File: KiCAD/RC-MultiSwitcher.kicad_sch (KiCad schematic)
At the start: 28 parts, among them IC1 LM2940IMP-5.0_NOPB, J1 Pwr_Outputs, J3 Srv_INPUTS, J4 Srv_OUTPUTS, Q1 DMG9926USD-13, Q2 DMG9926USD-13, Q3 DMG9926USD-13, U1 Teensy3.1

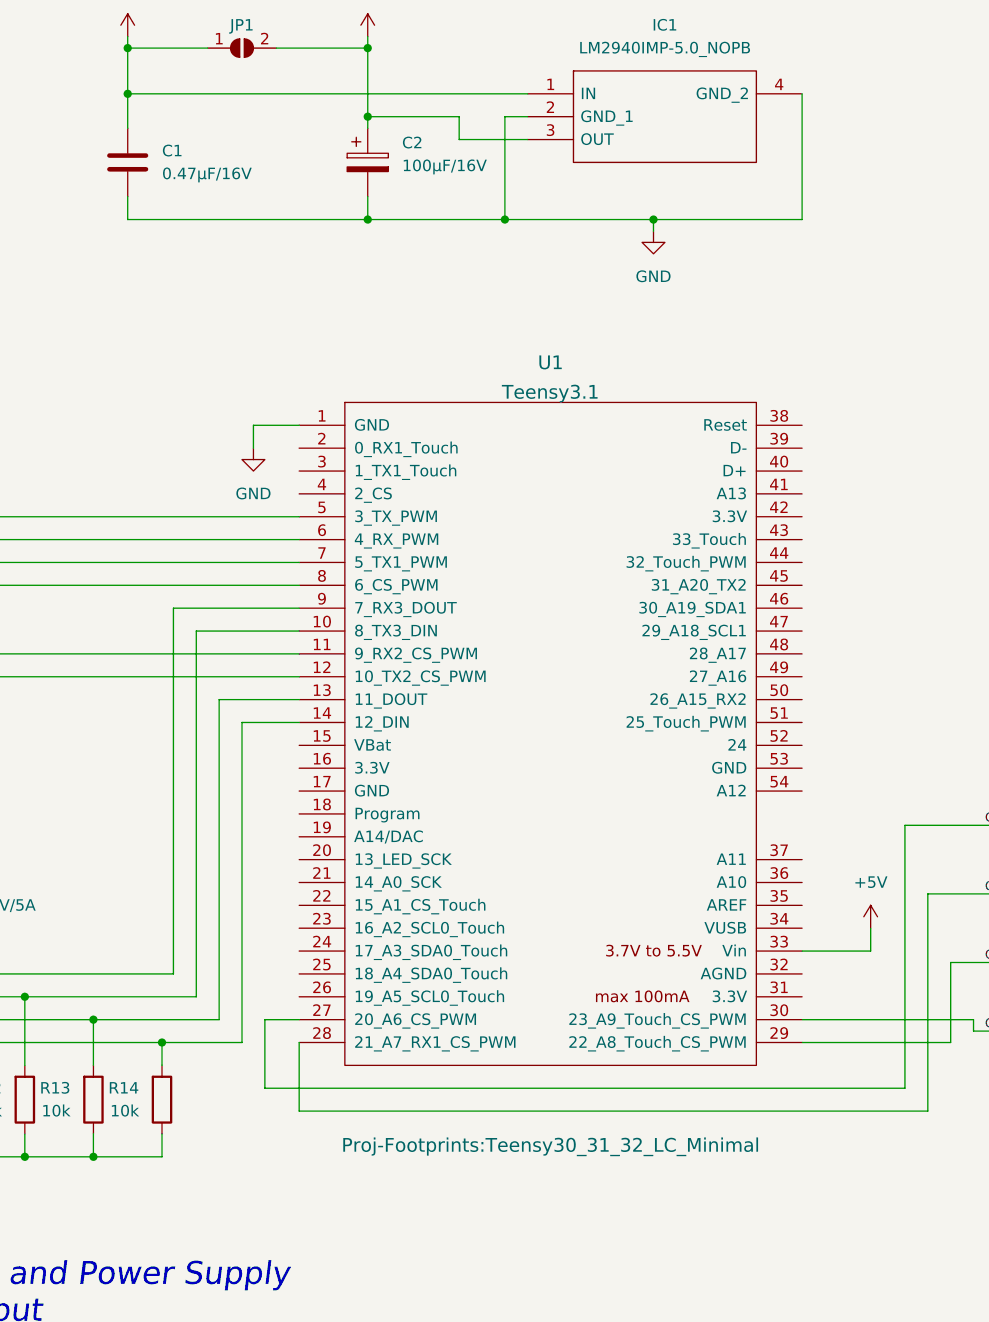
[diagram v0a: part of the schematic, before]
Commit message: minor layout improvements; added manufacturing data
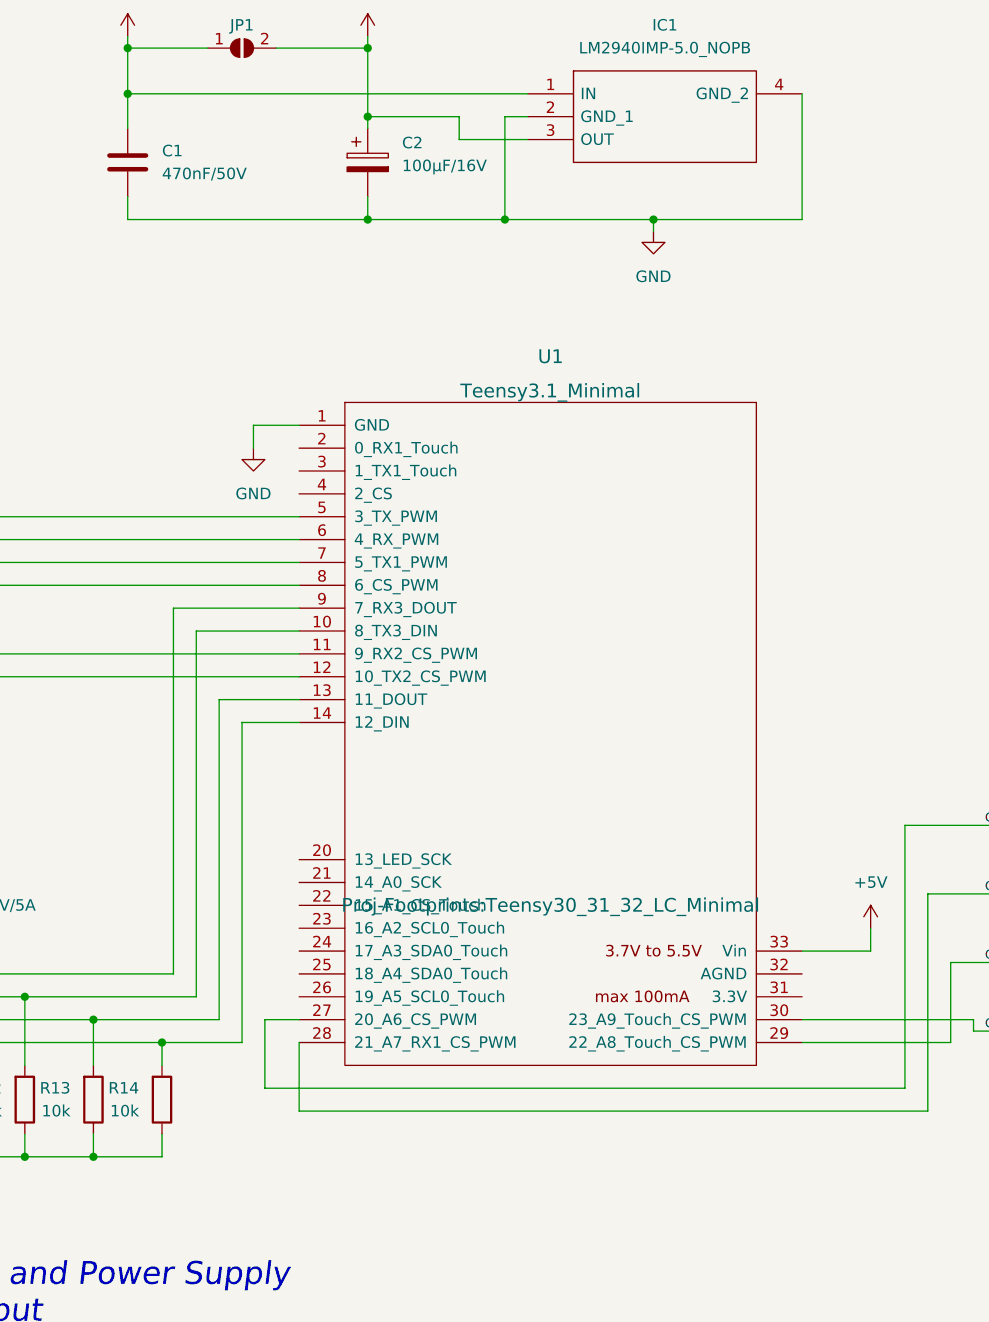
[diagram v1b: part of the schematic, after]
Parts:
- removed U1: Teensy3.1, Proj-Footprints:Teensy30_31_32_LC_Minimal, symbol Teensy3:Teensy3.1
- added U1: Teensy3.1_Minimal, Proj-Footprints:Teensy30_31_32_LC_Minimal, symbol Teensy3:Teensy3.1_Minimal
- C1: value 0.47µF/16V -> 470nF/50V; LCSC C106851 -> C77572
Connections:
- net +5V: now also U1.33 (Vin)
- net GND: now also U1.1 (GND)
- net I-SRV0: now also U1.9 (7_RX3_DOUT)
- net I-SRV1: now also U1.10 (8_TX3_DIN)
- net I-SRV2: now also U1.13 (11_DOUT)
- net I-SRV3: now also U1.14 (12_DIN)
- net O-SRV0: now also U1.27 (20_A6_CS_PWM)
- net O-SRV1: now also U1.28 (21_A7_RX1_CS_PWM)
- net O-SRV2: now also U1.29 (22_A8_Touch_CS_PWM)
- net O-SRV3: now also U1.30 (23_A9_Touch_CS_PWM)
- net at Q2.2 (G1), R3.2: now also U1.7 (5_TX1_PWM)
- net at Q3.4 (G2), R10.2: now also U1.12 (10_TX2_CS_PWM)
- net at Q3.2 (G1), R9.2: now also U1.11 (9_RX2_CS_PWM)
- net at Q1.2 (G1), R1.2: now also U1.5 (3_TX_PWM)
- net at Q1.4 (G2), R2.2: now also U1.6 (4_RX_PWM)
- net at Q2.4 (G2), R4.2: now also U1.8 (6_CS_PWM)

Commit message: minor update to PCB
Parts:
- added J2: Alt_Pwr, Connector_JST:JST_XH_B2B-XH-A_1x02_P2.50mm_Vertical, symbol Connector:Conn_01x02_Male
- added JP2: (no value), Jumper:SolderJumper-2_P1.3mm_Open_Pad1.0x1.5mm, symbol Jumper:SolderJumper_2_Open
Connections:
- net +6V: now also JP2.2 (B)
- net GND: now also J2.1 (Pin_1)
- net PWR-IN: now also J2.2 (Pin_2), JP2.1 (A)
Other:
- moved on the sheet: F1
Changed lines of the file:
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@@
   (junction (at 34.29 142.24) (diameter 0) (color 0 0 0 0)
   )
+  (junction (at 116.84 111.76) (diameter 0) (color 0 0 0 0)
+  )
   (junction (at 49.53 137.16) (diameter 0) (color 0 0 0 0)
   )
@@
   (junction (at 34.29 109.22) (diameter 0) (color 0 0 0 0)
   )
+  (junction (at 124.46 123.19) (diameter 0) (color 0 0 0 0)
+  )
   (junction (at 87.63 101.6) (diameter 0) (color 0 0 0 0)
   )
@@
   (junction (at 246.38 120.65) (diameter 0) (color 0 0 0 0)
   )
+  (junction (at 129.54 123.19) (diameter 0) (color 0 0 0 0)
+  )
   (junction (at 87.63 175.26) (diameter 0) (color 0 0 0 0)
   )
@@
   (junction (at 49.53 132.08) (diameter 0) (color 0 0 0 0)
   )
+  (wire (pts (xy 124.46 123.19) (xy 124.46 132.08))
+    (stroke (width 0) (type default) (color 0 0 0 0))
+  )
   (wire (pts (xy 248.92 106.68) (xy 248.92 115.57))
     (stroke (width 0) (type default) (color 0 0 0 0))
@@
     (stroke (width 0) (type default) (color 0 0 0 0))
   )
+  (wire (pts (xy 139.7 123.19) (xy 139.7 119.38))
+    (stroke (width 0) (type default) (color 0 0 0 0))
+  )
   (wire (pts (xy 87.63 83.82) (xy 162.56 83.82))
     (stroke (width 0) (type default) (color 0 0 0 0))
@@
     (stroke (width 0) (type default) (color 0 0 0 0))
   )
+  (wire (pts (xy 129.54 123.19) (xy 129.54 120.65))
+    (stroke (width 0) (type default) (color 0 0 0 0))
+  )
   (wire (pts (xy 52.07 170.18) (xy 49.53 170.18))
     (stroke (width 0) (type default) (color 0 0 0 0))
@@
     (stroke (width 0) (type default) (color 0 0 0 0))
   )
+  (wire (pts (xy 116.84 111.76) (xy 116.84 113.03))
+    (stroke (width 0) (type default) (color 0 0 0 0))
+  )
   (wire (pts (xy 251.46 118.11) (xy 229.87 118.11))
     (stroke (width 0) (type default) (color 0 0 0 0))
@@
     (stroke (width 0) (type default) (color 0 0 0 0))
   )
+  (wire (pts (xy 129.54 123.19) (xy 139.7 123.19))
+    (stroke (width 0) (type default) (color 0 0 0 0))
+  )
   (wire (pts (xy 80.01 106.68) (xy 77.47 106.68))
     (stroke (width 0) (type default) (color 0 0 0 0))
@@
     (stroke (width 0) (type default) (color 0 0 0 0))
   )
+  (wire (pts (xy 116.84 123.19) (xy 124.46 123.19))
+    (stroke (width 0) (type default) (color 0 0 0 0))
+  )
   (wire (pts (xy 78.74 170.18) (xy 77.47 170.18))
     (stroke (width 0) (type default) (color 0 0 0 0))
   )
+  (wire (pts (xy 129.54 111.76) (xy 116.84 111.76))
+    (stroke (width 0) (type default) (color 0 0 0 0))
+  )
   (wire (pts (xy 229.87 147.32) (xy 158.75 147.32))
     (stroke (width 0) (type default) (color 0 0 0 0))
@@
     (stroke (width 0) (type default) (color 0 0 0 0))
   )
+  (wire (pts (xy 142.24 119.38) (xy 142.24 127))
+    (stroke (width 0) (type default) (color 0 0 0 0))
+  )
   (wire (pts (xy 234.95 142.24) (xy 218.44 142.24))
     (stroke (width 0) (type default) (color 0 0 0 0))
@@
     (stroke (width 0) (type default) (color 0 0 0 0))
   )
-  (wire (pts (xy 124.46 132.08) (xy 124.46 129.54))
+  (wire (pts (xy 116.84 123.19) (xy 116.84 120.65))
     (stroke (width 0) (type default) (color 0 0 0 0))
   )
@@
     (stroke (width 0) (type default) (color 0 0 0 0))
   )
+  (wire (pts (xy 129.54 113.03) (xy 129.54 111.76))
+    (stroke (width 0) (type default) (color 0 0 0 0))
+  )
   (wire (pts (xy 21.59 132.08) (xy 29.21 132.08))
     (stroke (width 0) (type default) (color 0 0 0 0))
@@
     (stroke (width 0) (type default) (color 0 0 0 0))
   )
-  (wire (pts (xy 124.46 119.38) (xy 124.46 121.92))
+  (wire (pts (xy 116.84 110.49) (xy 116.84 111.76))
     (stroke (width 0) (type default) (color 0 0 0 0))
   )
@@
     (stroke (width 0) (type default) (color 0 0 0 0))
   )
+  (wire (pts (xy 124.46 123.19) (xy 129.54 123.19))
+    (stroke (width 0) (type default) (color 0 0 0 0))
+  )
   (wire (pts (xy 52.07 134.62) (xy 49.53 134.62))
     (stroke (width 0) (type default) (color 0 0 0 0))
@@
     (pin "2")
   )
-  (symbol (lib_id "power:+6V") (at 124.46 119.38 0) (unit 1)
+  (symbol (lib_id "power:+6V") (at 116.84 110.49 0) (unit 1)
     (in_bom yes) (on_board yes) (fields_autoplaced)
-    (property "Reference" "#PWR0114" (id 0) (at 124.46 123.19 0)
+    (property "Reference" "#PWR0114" (id 0) (at 116.84 114.3 0)
       (effects (font (size 1.27 1.27)) hide)
     )
-    (property "Value" "+6V" (id 1) (at 124.46 114.3 0))
-    (property "Footprint" "" (id 2) (at 124.46 119.38 0)
+    (property "Value" "+6V" (id 1) (at 116.84 105.41 0))
+    (property "Footprint" "" (id 2) (at 116.84 110.49 0)
       (effects (font (size 1.27 1.27)) hide)
     )
-    (property "Datasheet" "" (id 3) (at 124.46 119.38 0)
+    (property "Datasheet" "" (id 3) (at 116.84 110.49 0)
       (effects (font (size 1.27 1.27)) hide)
     )
@@
     (pin "1")
   )
-  (symbol (lib_id "Device:Polyfuse") (at 124.46 125.73 0) (unit 1)
+  (symbol (lib_id "Device:Polyfuse") (at 116.84 116.84 0) (unit 1)
     (in_bom yes) (on_board yes) (fields_autoplaced)
-    (property "Reference" "F1" (id 0) (at 127 124.4599 0)
+    (property "Reference" "F1" (id 0) (at 119.38 115.5699 0)
       (effects (font (size 1.27 1.27)) (justify left))
     )
-    (property "Value" "16V/5A" (id 1) (at 127 126.9999 0)
+    (property "Value" "16V/5A" (id 1) (at 119.38 118.1099 0)
       (effects (font (size 1.27 1.27)) (justify left))
     )
-    (property "Footprint" "Fuse:Fuse_1812_4532Metric" (id 2) (at 125.73 130.81 0)
+    (property "Footprint" "Fuse:Fuse_1812_4532Metric" (id 2) (at 118.11 121.92 0)
       (effects (font (size 1.27 1.27)) (justify left) hide)
     )
-    (property "Datasheet" "~" (id 3) (at 124.46 125.73 0)
+    (property "Datasheet" "~" (id 3) (at 116.84 116.84 0)
       (effects (font (size 1.27 1.27)) hide)
     )
-    (property "LCSC" "C55996" (id 4) (at 124.46 125.73 0)
+    (property "LCSC" "C55996" (id 4) (at 116.84 116.84 0)
       (effects (font (size 1.27 1.27)) hide)
     )
@@
     (pin "9")
   )
+  (symbol (lib_id "power:GND") (at 142.24 127 0) (unit 1)
+    (in_bom yes) (on_board yes) (fields_autoplaced)
+    (property "Reference" "#PWR01" (id 0) (at 142.24 133.35 0)
+      (effects (font (size 1.27 1.27)) hide)
+    )
+    (property "Value" "GND" (id 1) (at 142.24 131.5625 0))
+    (property "Footprint" "" (id 2) (at 142.24 127 0)
+      (effects (font (size 1.27 1.27)) hide)
+    )
+    (property "Datasheet" "" (id 3) (at 142.24 127 0)
+      (effects (font (size 1.27 1.27)) hide)
+    )
+    (pin "1")
+  )
   (symbol (lib_id "Connector:Conn_01x12_Male") (at 16.51 121.92 0) (unit 1)
     (in_bom yes) (on_board yes)
@@
     (pin "1")
   )
+  (symbol (lib_id "Connector:Conn_01x02_Male") (at 142.24 114.3 270) (unit 1)
+    (in_bom yes) (on_board yes)
+    (property "Reference" "J2" (id 0) (at 139.7 110.49 90)
+      (effects (font (size 1.27 1.27)) (justify left))
+    )
+    (property "Value" "Alt_Pwr" (id 1) (at 137.16 113.03 90)
+      (effects (font (size 1.27 1.27)) (justify left))
+    )
+    (property "Footprint" "Connector_JST:JST_XH_B2B-XH-A_1x02_P2.50mm_Vertical" (id 2) (at 142.24 114.3 0)
+      (effects (font (size 1.27 1.27)) hide)
+    )
+    (property "Datasheet" "~" (id 3) (at 142.24 114.3 0)
+      (effects (font (size 1.27 1.27)) hide)
+    )
+    (property "LCSC" "DNP" (id 4) (at 142.24 114.3 90)
+      (effects (font (size 1.27 1.27)) hide)
+    )
+    (pin "1")
+    (pin "2")
+  )
   (symbol (lib_id "Device:R") (at 87.63 161.29 0) (mirror x) (unit 1)
     (in_bom yes) (on_board yes) (fields_autoplaced)
@@
     (pin "2")
   )
+  (symbol (lib_id "Jumper:SolderJumper_2_Open") (at 129.54 116.84 90) (unit 1)
+    (in_bom yes) (on_board yes)
+    (property "Reference" "JP2" (id 0) (at 133.35 116.84 90))
+    (property "Value" " " (id 1) (at 125.73 116.84 0))
+    (property "Footprint" "Jumper:SolderJumper-2_P1.3mm_Open_Pad1.0x1.5mm" (id 2) (at 129.54 116.84 0)
+      (effects (font (size 1.27 1.27)) hide)
+    )
+    (property "Datasheet" "~" (id 3) (at 129.54 116.84 0)
+      (effects (font (size 1.27 1.27)) hide)
+    )
+    (pin "1")
+    (pin "2")
+  )
   (symbol (lib_id "Jumper:SolderJumper_2_Open") (at 156.21 31.75 0) (unit 1)
     (in_bom yes) (on_board yes)
@@
   )
   (symbol_instances
+    (path "/9a33edd1-6244-4512-a518-ef52d175a483"
+      (reference "#PWR01") (unit 1) (value "GND") (footprint "")
+    )
     (path "/e7829832-4149-4a45-b712-a23fe318d1fa"
       (reference "#PWR0101") (unit 1) (value "GND") (footprint "")
@@
       (reference "J1") (unit 1) (value "Pwr_Outputs") (footprint "Connector_PinHeader_2.54mm:PinHeader_1x12_P2.54mm_Vertical")
     )
+    (path "/dbdd97d7-be61-49ca-a40b-ac35c0a2d7e6"
+      (reference "J2") (unit 1) (value "Alt_Pwr") (footprint "Connector_JST:JST_XH_B2B-XH-A_1x02_P2.50mm_Vertical")
+    )
     (path "/3048991f-bdac-442e-96d7-53774eecf9f0"
       (reference "J3") (unit 1) (value "Srv_INPUTS") (footprint "Connector_PinHeader_2.54mm:PinHeader_1x06_P2.54mm_Vertical")
@@
       (reference "JP1") (unit 1) (value " ") (footprint "Jumper:SolderJumper-2_P1.3mm_Open_Pad1.0x1.5mm")
     )
+    (path "/fa2a5346-d622-407d-8ea5-af43140584bc"
+      (reference "JP2") (unit 1) (value " ") (footprint "Jumper:SolderJumper-2_P1.3mm_Open_Pad1.0x1.5mm")
+    )
     (path "/d19210a8-a885-4536-b0bf-62394b9670d1"

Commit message: major code updates
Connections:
- net SW6 is gone; now on net SW5: D6.2 (A), J1.11 (Pin_11), Q3.5 (D2_1), Q3.6 (D2_2)
- net SW1: now also D2.2 (A), J1.3 (Pin_3), Q1.5 (D2_1), Q1.6 (D2_2); no longer D1.2 (A), J1.1 (Pin_1), Q1.7 (D1_1), Q1.8 (D1_2)
- net SW2: now also D3.2 (A), J1.5 (Pin_5), Q2.7 (D1_1), Q2.8 (D1_2); no longer D2.2 (A), J1.3 (Pin_3), Q1.5 (D2_1), Q1.6 (D2_2)
- net SW3: now also D4.2 (A), J1.7 (Pin_7), Q2.5 (D2_1), Q2.6 (D2_2); no longer D3.2 (A), J1.5 (Pin_5), Q2.7 (D1_1), Q2.8 (D1_2)
- net SW4: now also D5.2 (A), J1.9 (Pin_9), Q3.7 (D1_1), Q3.8 (D1_2); no longer D4.2 (A), J1.7 (Pin_7), Q2.5 (D2_1), Q2.6 (D2_2)
- net SW5: no longer D5.2 (A), J1.9 (Pin_9), Q3.7 (D1_1), Q3.8 (D1_2)
- new net SW0: D1.2 (A), J1.1 (Pin_1), Q1.7 (D1_1), Q1.8 (D1_2)
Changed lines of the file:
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@@
     (effects (font (size 2.54 2.54) italic) (justify left bottom))
   )
-  (label "SW1" (at 44.45 99.06 0)
+  (label "SW0" (at 44.45 99.06 0)
     (effects (font (size 1 1)) (justify left bottom))
   )
@@
     (effects (font (size 1 1)) (justify left bottom))
   )
-  (label "SW3" (at 44.45 119.38 0)
+  (label "SW2" (at 44.45 119.38 0)
     (effects (font (size 1 1)) (justify left bottom))
   )
@@
     (effects (font (size 1 1)) (justify left bottom))
   )
-  (label "SW2" (at 44.45 109.22 0)
+  (label "SW1" (at 44.45 109.22 0)
     (effects (font (size 1 1)) (justify left bottom))
   )
@@
     (effects (font (size 1 1)) (justify left bottom))
   )
-  (label "SW5" (at 44.45 142.24 0)
+  (label "SW4" (at 44.45 142.24 0)
     (effects (font (size 1 1)) (justify left bottom))
   )
@@
     (effects (font (size 1 1)) (justify left bottom))
   )
-  (label "SW4" (at 44.45 130.81 0)
+  (label "SW3" (at 44.45 130.81 0)
     (effects (font (size 1 1)) (justify left bottom))
   )
-  (label "SW6" (at 44.45 167.64 0)
+  (label "SW5" (at 44.45 167.64 0)
     (effects (font (size 1 1)) (justify left bottom))
   )
